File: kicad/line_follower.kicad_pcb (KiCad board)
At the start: 2 copper layers, 80 x 100 mm, 39 parts, among them J1 XT30PW-M, M1 MOTOR_ENC, M2 MOTOR_ENC, Q1 ALS-PT19-315C_L177_TR8, Q2 ALS-PT19-315C_L177_TR8, Q3 ALS-PT19-315C_L177_TR8, Q4 ALS-PT19-315C_L177_TR8, Q5 ALS-PT19-315C_L177_TR8, SW1 SW_Push, U1 A4950E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

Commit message: Getting there with the PCB design.
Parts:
- added HS1: Heatsink_Pad, cube-library:3x3_thermal_vias, F.Cu at (22.9, 1.27)
- added HS2: Heatsink_Pad, cube-library:3x3_thermal_vias, F.Cu at (-12.7, 1.27)
- added HS3: Heatsink_Pad, cube-library:3x3_thermal_vias, F.Cu at (-22.9, 1.27)
- added HS4: Heatsink_Pad, cube-library:3x3_thermal_vias, F.Cu at (12.7, 1.27)
- moved R7 43.2 mm to (21.6, 41.9), turned to 0 degrees
- moved C10 39.2 mm to (-31.8, 38.1)
- moved R6 38.3 mm to (16.5, 41.9)
- moved C11 30.3 mm to (-31.8, 27.9)
- moved U3 29.8 mm to (-31.8, 33.0), turned to 0 degrees
- moved X3 26.9 mm to (29.2, 58.4), turned to 90 degrees
- moved M2 22.2 mm to (-14.0, -8.26)
- moved M1 21.9 mm to (14.0, -8.26)
- moved C6 20.1 mm to (12.7, -2.54), turned to 270 degrees
- moved C9 12.8 mm to (-5.71, -1.27), turned to 180 degrees
- moved U2 10.8 mm to (-17.8, 0.00), turned to 90 degrees
- moved D1 10.8 mm to (24.7, 78.2)
- moved R1 10.2 mm to (21.6, 58.4)
- moved R2 10.2 mm to (16.5, 58.4)
- moved R3 10.2 mm to (11.4, 58.4)
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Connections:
- net /LINE_SENSOR1 renamed LINE_SENSOR1
- net /LINE_SENSOR2 renamed LINE_SENSOR2
- C1 pad 2: /LINE_SENSOR0 -> LINE_SENSOR0
- C4 pad 2: /LINE_SENSOR3 -> LINE_SENSOR3
- C5 pad 2: /LINE_SENSOR4 -> LINE_SENSOR4
- D1 pad 1: /LINE_LED1 -> LINE_LED1
- D1 pad 2: /LINE_LED0 -> LINE_LED0
- D2 pad 1: /LINE_LED0 -> LINE_LED0
- D2 pad 2: /LINE_LED1 -> LINE_LED1
- D3 pad 1: /LINE_LED2 -> LINE_LED2
- D3 pad 2: /LINE_LED0 -> LINE_LED0
- D4 pad 1: /LINE_LED0 -> LINE_LED0
- D4 pad 2: /LINE_LED2 -> LINE_LED2
- D5 pad 1: /LINE_LED1 -> LINE_LED1
- D5 pad 2: /LINE_LED2 -> LINE_LED2
- D6 pad 1: /LINE_LED2 -> LINE_LED2
- D6 pad 2: /LINE_LED1 -> LINE_LED1
- Q1 pad 2: /LINE_SENSOR0 -> LINE_SENSOR0
- Q4 pad 2: /LINE_SENSOR3 -> LINE_SENSOR3
- Q5 pad 2: /LINE_SENSOR4 -> LINE_SENSOR4
- R1 pad 2: /LINE_SENSOR0 -> LINE_SENSOR0
- R4 pad 2: /LINE_SENSOR3 -> LINE_SENSOR3
- R5 pad 2: /LINE_SENSOR4 -> LINE_SENSOR4
- U1 pad 4: +5V -> +3V3
- U2 pad 4: +5V -> +3V3
- X1 pad 10: /LINE_LED2 -> LINE_LED0
- X1 pad 11: /LINE_SENSOR3 -> /RANGE
- X1 pad 12: /MOTOR2A -> /MOTOR1B
- X1 pad 13: /MOTOR2B -> /MOTOR1A
- X1 pad 2: /ENCODER1B -> /ENCODER2A
- X1 pad 21: /ENCODER2B -> /ENCODER1A
- X1 pad 22: /ENCODER2A -> /ENCODER1B
- X1 pad 25: /MOTOR1A -> /MOTOR2B
- X1 pad 3: /ENCODER1A -> /ENCODER2B
- X1 pad 30: /MOTOR1B -> /MOTOR2A
- X1 pad 4: /LINE_SENSOR0 -> LINE_SENSOR4
- X1 pad 5: /RANGE -> LINE_SENSOR3
- X1 pad 7: /LINE_SENSOR4 -> LINE_SENSOR0
- X1 pad 8: /LINE_LED0 -> LINE_LED1
- X1 pad 9: /LINE_LED1 -> LINE_LED2
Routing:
- net GND: track 0.00 -> 415.5 mm, vias 0 -> 3
- net +3V3: track 0.00 -> 228.1 mm, vias 0 -> 7
- net +BATT: track 0.00 -> 187.5 mm, vias 0 -> 4
- net +5V: track 0.00 -> 142.3 mm
- net /ENCODER2A: track 0.00 -> 102.5 mm
- net /ENCODER2B: track 0.00 -> 101.1 mm
- net /MOTOR1A: track 0.00 -> 69.6 mm, vias 0 -> 1
- net /MOTOR1B: track 0.00 -> 69.1 mm, vias 0 -> 1
- net LINE_LED1: track 0.00 -> 68.2 mm, vias 0 -> 4
- net LINE_LED2: track 0.00 -> 62.7 mm, vias 0 -> 4
- net LINE_LED0: track 0.00 -> 61.7 mm, vias 0 -> 4
- net /ENCODER1A: track 0.00 -> 57.7 mm
- net /ENCODER1B: track 0.00 -> 56.6 mm
- net /MOTOR2B: track 0.00 -> 56.5 mm
- net /MOTOR2A: track 0.00 -> 45.8 mm
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- added copper zone on B.Cu, net GND
- added copper zone on F.Cu, net GND
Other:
- outline, holes or cut-outs redrawn

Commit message: Board done except for the motor mounts
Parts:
- added H1: MountingHole, MountingHole:MountingHole_3.2mm_M3, F.Cu at (0.00, -8.26)
- added H2: MountingHole, MountingHole:MountingHole_3.2mm_M3, F.Cu at (-29.8, -6.35)
- added H3: MountingHole, MountingHole:MountingHole_3.2mm_M3, F.Cu at (-29.2, 11.4)
- added H4: MountingHole, MountingHole:MountingHole_3.2mm_M3, F.Cu at (29.2, -6.35)
- added H5: MountingHole, MountingHole:MountingHole_3.2mm_M3, F.Cu at (29.2, 10.8)
- M1, M2: footprint cube-library:SolderWirePad1x6_p2.54 -> cube-library:SolderWirePad2x3_p2.54_staggered
- moved R6 8.89 mm to (16.5, 50.8)
- moved R7 8.89 mm to (21.6, 50.8)
- moved C8 5.08 mm to (5.71, 3.81), turned to 270 degrees
- moved C9 5.08 mm to (-5.71, 3.81), turned to 270 degrees
- moved M2 3.86 mm to (-17.8, -8.89)
- moved M1 2.62 mm to (16.5, -8.89)
- moved SW1 1.27 mm to (0.00, 7.62), turned to 270 degrees
- moved C10 0.63 mm to (-32.4, 38.1)
- moved C11 0.63 mm to (-32.4, 27.9)
- renumbered HS4 to HS2, HS2 to HS4
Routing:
- net GND: track 415.5 -> 381.6 mm, vias 3 -> 5
- net +3V3: track 228.1 -> 213.4 mm, vias 7 -> 5
- net +BATT: track 187.5 -> 178.9 mm
- net /ENCODER1B: track 56.6 -> 64.3 mm
- net Net-(M2-Pad6): track 12.0 -> 5.61 mm
- net /ENCODER1A: track 57.7 -> 63.2 mm
- net Net-(M1-Pad1): track 13.9 -> 8.76 mm
- net /BUTTON: track 42.1 -> 44.1 mm
- net Net-(M2-Pad1): track 5.61 -> 7.41 mm
- net LINE_LED0: track 61.7 -> 59.9 mm
- net LINE_LED2: track 62.7 -> 61.2 mm
- net /ACCEL_INT: track 28.0 -> 29.5 mm
- net +5V: track 142.3 -> 140.9 mm
- net /MOTOR1B: track 69.1 -> 70.4 mm
- net /BAT_SENSE: track 6.84 -> 8.11 mm
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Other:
- board text added: "6V-17V (2S-4S LiPo)"
- board text added: "JLCJLCJLCJLC"
- board text added: "Line Follower v2 https://github.com/bluecube August 2020"

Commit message: Small PCB tweaks
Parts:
- moved C6 1.27 mm to (14.0, -2.54)
- moved HS4 1.27 mm to (-14.0, 1.27)
- moved C7 1.27 mm to (-24.1, -2.54)
- moved HS1 1.27 mm to (24.1, 1.27)
- moved HS3 1.27 mm to (-24.1, 1.27)
- moved M1 1.27 mm to (17.8, -8.89)
- moved M2 1.27 mm to (-19.1, -8.89)
- moved U1 1.27 mm to (19.1, 0.00)
- moved U2 1.27 mm to (-19.1, 0.00)
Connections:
- J1 pad 3: Net-(J1-Pad3) -> GND
- J1 pad 4: Net-(J1-Pad4) -> GND
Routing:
- net GND: track 381.6 -> 418.2 mm, vias 5 -> 4
- net +BATT: track 178.9 -> 181.4 mm
- net /ENCODER2A: track 103.1 -> 104.4 mm
- net /ENCODER1B: track 64.3 -> 65.6 mm
- net /ENCODER1A: track 63.2 -> 64.5 mm
- net /ENCODER2B: track 101.7 -> 103.0 mm
- net +3V3: track 213.4 -> 214.2 mm
- net /ACCEL_INT: track 29.5 -> 28.8 mm
- net /MOTOR1A: track 69.6 -> 69.1 mm
- net /MOTOR2A: track 45.8 -> 46.3 mm
- net /MOTOR2B: track 55.8 -> 56.3 mm

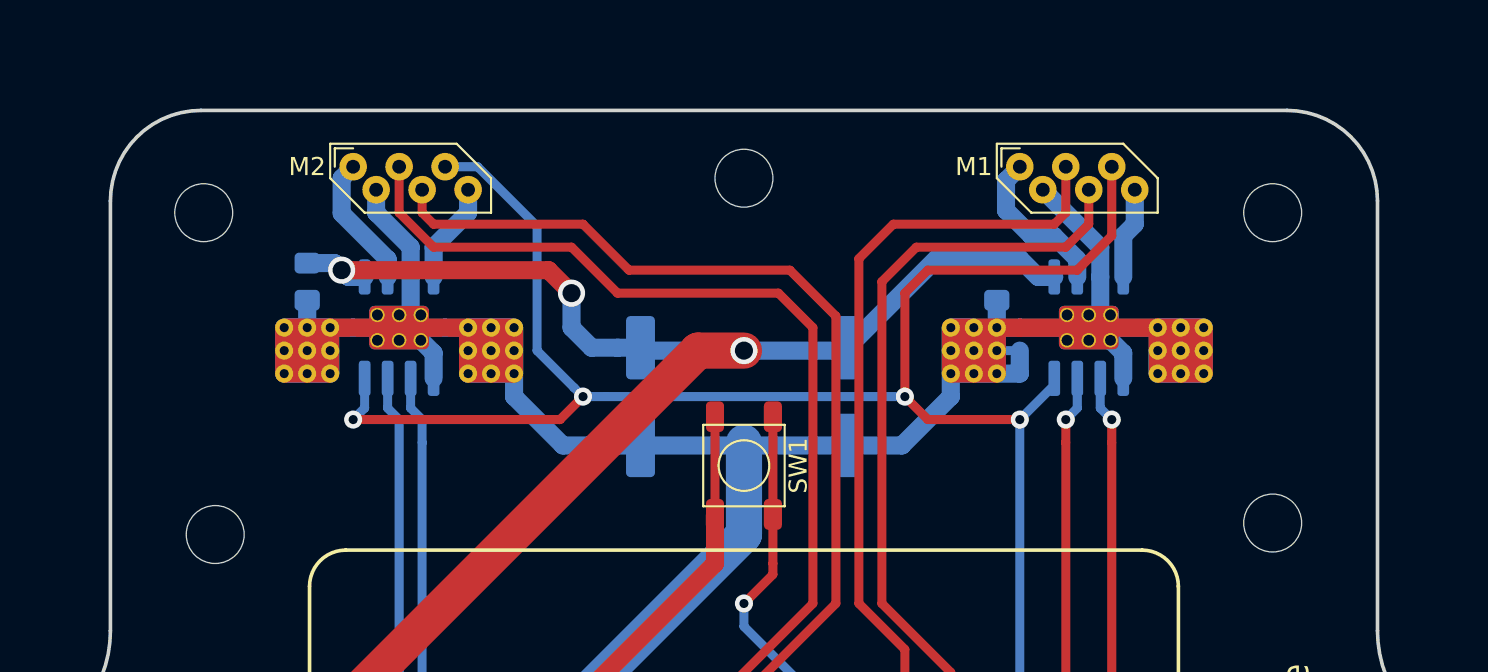
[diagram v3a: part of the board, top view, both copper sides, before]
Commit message: Placed motor mounting holes and silkscreen outlines.
Board done for now.
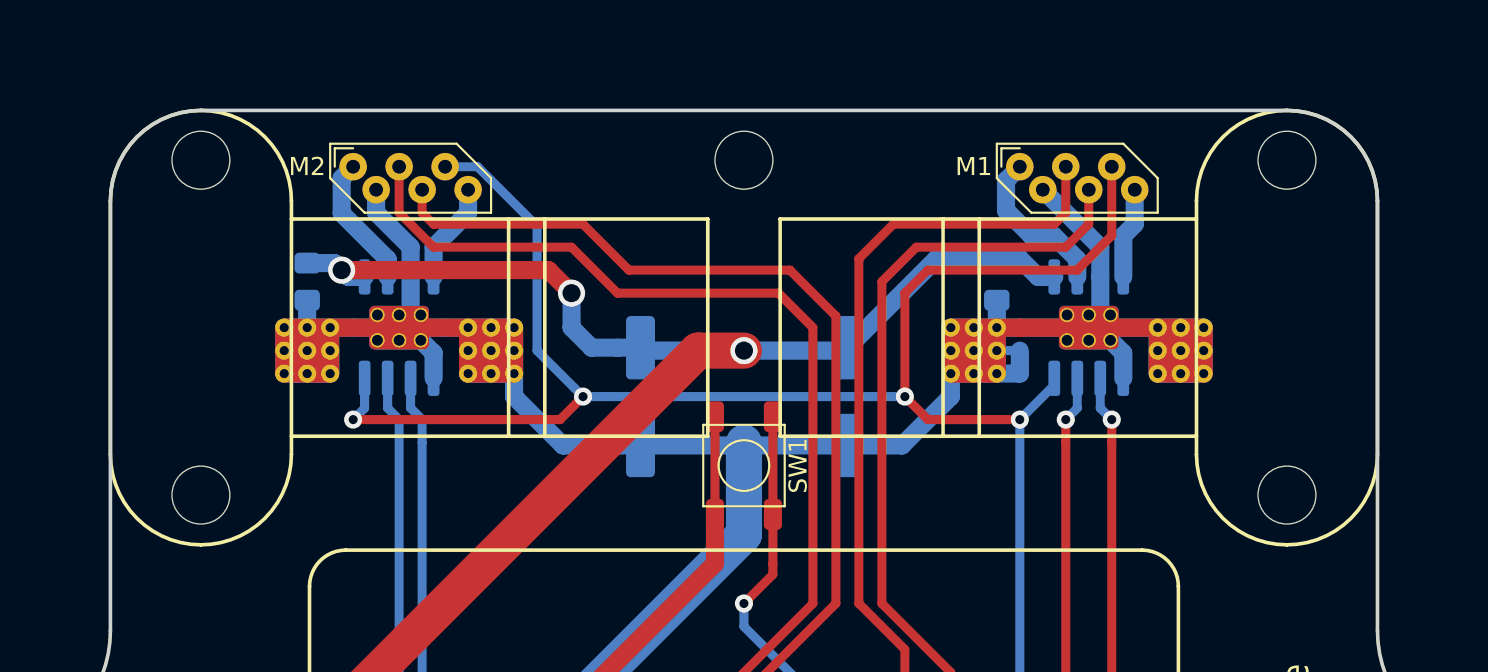
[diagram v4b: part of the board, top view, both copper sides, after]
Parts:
- moved H4 3.01 mm to (30.0, -9.25)
- moved H2 2.90 mm to (-30.0, -9.25)
- moved H3 2.32 mm to (-30.0, 9.25)
- moved H5 1.74 mm to (30.0, 9.25)
- moved H1 0.99 mm to (0.00, -9.25)
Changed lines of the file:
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@@
   (general
     (thickness 1.6)
-    (drawings 33)
+    (drawings 59)
     (tracks 499)
     (zones 0)
@@
   )
   (module MountingHole:MountingHole_3.2mm_M3 (layer F.Cu)
-    (at -29.845 -6.35)
+    (at -30 -9.25)
     (descr "Mounting Hole 3.2mm, no annular, M3")
     (tags "mounting hole 3.2mm no annular m3")
@@
   )
   (module MountingHole:MountingHole_3.2mm_M3 (layer F.Cu)
-    (at -29.21 11.43)
+    (at -30 9.25)
     (descr "Mounting Hole 3.2mm, no annular, M3")
     (tags "mounting hole 3.2mm no annular m3")
@@
   )
   (module MountingHole:MountingHole_3.2mm_M3 (layer F.Cu)
-    (at 29.21 -6.35)
+    (at 30 -9.25)
     (descr "Mounting Hole 3.2mm, no annular, M3")
     (tags "mounting hole 3.2mm no annular m3")
@@
   )
   (module MountingHole:MountingHole_3.2mm_M3 (layer F.Cu)
-    (at 29.21 10.795)
+    (at 30 9.25)
     (descr "Mounting Hole 3.2mm, no annular, M3")
     (tags "mounting hole 3.2mm no annular m3")
@@
   )
   (module MountingHole:MountingHole_3.2mm_M3 (layer F.Cu)
-    (at 0 -8.255)
+    (at 0 -9.25)
     (descr "Mounting Hole 3.2mm, no annular, M3")
     (tags "mounting hole 3.2mm no annular m3")
@@
       (net 11 "Net-(M2-Pad1)"))
   )
+  (gr_arc (start 30 6.999999) (end 30 11.999999) (angle -90) (layer F.SilkS) (width 0.2))
+  (gr_line (start 35 6.999999) (end 35 -7) (layer F.SilkS) (width 0.2))
+  (gr_arc (start 30 -7) (end 35 -7) (angle -90) (layer F.SilkS) (width 0.2))
+  (gr_line (start 25 -7) (end 25 6.999999) (layer F.SilkS) (width 0.2))
+  (gr_arc (start 30 6.999999) (end 25 6.999999) (angle -90) (layer F.SilkS) (width 0.2))
+  (gr_arc (start 30 -7) (end 30 -12) (angle -90) (layer F.SilkS) (width 0.2))
+  (gr_line (start 25 -6) (end 12.999999 -6) (layer F.SilkS) (width 0.2))
+  (gr_line (start 12.999999 -6) (end 10.999999 -6) (layer F.SilkS) (width 0.2))
+  (gr_line (start 12.999999 6) (end 12.999999 -6) (layer F.SilkS) (width 0.2))
+  (gr_line (start 10.999999 -6) (end 10.999999 6) (layer F.SilkS) (width 0.2))
+  (gr_line (start 1.999999 6) (end 24.999999 6) (layer F.SilkS) (width 0.2))
+  (gr_line (start 1.999999 -6) (end 1.999999 6) (layer F.SilkS) (width 0.2))
+  (gr_line (start 10.999999 -6) (end 1.999999 -6) (layer F.SilkS) (width 0.2))
+  (gr_line (start -12.999999 -6) (end -10.999999 -6) (layer F.SilkS) (width 0.2))
+  (gr_line (start -25 -7) (end -25 6.999999) (layer F.SilkS) (width 0.2))
+  (gr_line (start -10.999999 -6) (end -1.999999 -6) (layer F.SilkS) (width 0.2))
+  (gr_line (start -25 -6) (end -12.999999 -6) (layer F.SilkS) (width 0.2))
+  (gr_line (start -12.999999 6) (end -12.999999 -6) (layer F.SilkS) (width 0.2))
+  (gr_line (start -10.999999 -6) (end -10.999999 6) (layer F.SilkS) (width 0.2))
+  (gr_line (start -35 6.999999) (end -35 -7) (layer F.SilkS) (width 0.2))
+  (gr_line (start -1.999999 6) (end -24.999999 6) (layer F.SilkS) (width 0.2))
+  (gr_line (start -1.999999 -6) (end -1.999999 6) (layer F.SilkS) (width 0.2))
+  (gr_arc (start -30 6.999999) (end -30 11.999999) (angle -90) (layer F.SilkS) (width 0.2))
+  (gr_arc (start -30 6.999999) (end -35 6.999999) (angle -90) (layer F.SilkS) (width 0.2))
+  (gr_arc (start -30 -7) (end -25 -7) (angle -90) (layer F.SilkS) (width 0.2))
+  (gr_arc (start -30 -7) (end -30 -12) (angle -90) (layer F.SilkS) (width 0.2))
   (gr_text "6V-17V\n(2S-4S LiPo)" (at -31.75 34.29 90) (layer F.SilkS)
     (effects (font (size 1.5 1.2) (thickness 0.25)) (justify left))

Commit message: Untangled routing at the front of the robot a bit, moved battery location
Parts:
- moved SW1 1.38 mm to (0.00, 9.00), turned to 180 degrees
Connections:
- X1 pad 11: /RANGE -> LINE_SENSOR1
- X1 pad 12: /MOTOR1B -> LINE_SENSOR3
- X1 pad 20: LINE_SENSOR1 -> /MOTOR1B
- X1 pad 5: LINE_SENSOR3 -> LINE_SENSOR2
- X1 pad 6: LINE_SENSOR2 -> LINE_LED1
- X1 pad 8: LINE_LED1 -> /RANGE
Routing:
- net /MOTOR1B: track 70.4 -> 44.8 mm
- net LINE_SENSOR1: track 42.2 -> 24.7 mm, vias 1 -> 0
- net LINE_SENSOR3: track 31.0 -> 48.0 mm, vias 0 -> 1
- net GND: track 418.2 -> 433.6 mm, vias 4 -> 8
- net /RANGE: track 27.5 -> 35.1 mm
- net LINE_SENSOR0: track 45.6 -> 40.5 mm
- net LINE_SENSOR2: track 30.3 -> 32.8 mm
- net /ENCODER1B: track 65.6 -> 63.4 mm
- net /BUTTON: track 44.1 -> 42.2 mm
- net /ENCODER1A: track 64.5 -> 62.9 mm
- net /ENCODER2B: track 103.0 -> 104.0 mm
- net /ENCODER2A: track 104.4 -> 105.5 mm

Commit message: board: A bit more tweaking
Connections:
- X1 pad 12: LINE_SENSOR3 -> /RANGE
- X1 pad 8: /RANGE -> LINE_SENSOR3
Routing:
- net LINE_SENSOR3: track 48.0 -> 37.9 mm
- net /RANGE: track 35.1 -> 25.0 mm
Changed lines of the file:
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@@
     (thickness 1.6)
     (drawings 59)
-    (tracks 503)
+    (tracks 500)
     (zones 0)
     (modules 48)
@@
       (net 14 /BUTTON))
     (pad 8 thru_hole oval (at 0 12.7) (size 1.2 2) (drill 0.9) (layers *.Cu *.Mask)
-      (net 24 /RANGE))
+      (net 33 LINE_SENSOR3))
     (pad 22 thru_hole oval (at 2.54 -12.7) (size 1.2 2) (drill 0.9) (layers *.Cu *.Mask)
       (net 8 /ENCODER1B))
@@
       (net 26 "Net-(X1-Pad19)"))
     (pad 12 thru_hole oval (at 10.16 12.7) (size 1.2 2) (drill 0.9) (layers *.Cu *.Mask)
-      (net 33 LINE_SENSOR3))
+      (net 24 /RANGE))
     (pad 18 thru_hole oval (at 12.7 -12.7) (size 1.2 2) (drill 0.9) (layers *.Cu *.Mask)
       (net 13 /BAT_SENSE))
@@
   (gr_arc (start -41.75 16.749999) (end -38.857142 22.848678) (angle -64.62306647) (layer Edge.Cuts) (width 0.2))
   (gr_line (start -35 -7) (end -35 16.749999) (layer Edge.Cuts) (width 0.2))
-  (via (at -2.54 77.47) (size 1) (drill 0.5) (layers F.Cu B.Cu) (net 1))
+  (via (at -2.54 76.835) (size 1) (drill 0.5) (layers F.Cu B.Cu) (net 1))
   (via (at -11.43 76.2) (size 1) (drill 0.5) (layers F.Cu B.Cu) (net 1))
   (segment (start -30.725 31.945) (end -29.65 33.02) (width 1) (layer B.Cu) (net 1))
@@
   (via (at -5.08 63.5) (size 1) (drill 0.5) (layers F.Cu B.Cu) (net 23))
   (segment (start 26.67 68.58) (end 26.67 72.39) (width 0.5) (layer F.Cu) (net 24))
-  (segment (start 25.4 73.66) (end 11.43 73.66) (width 0.5) (layer F.Cu) (net 24))
   (segment (start 26.67 72.39) (end 25.4 73.66) (width 0.5) (layer F.Cu) (net 24))
-  (segment (start 7.62 73.66) (end 11.43 73.66) (width 0.5) (layer F.Cu) (net 24))
   (segment (start 29.21 60.96) (end 29.21 66.04) (width 0.5) (layer F.Cu) (net 24))
   (segment (start 29.21 66.04) (end 26.67 68.58) (width 0.5) (layer F.Cu) (net 24))
-  (segment (start 6.35 72.39) (end 7.62 73.66) (width 0.5) (layer F.Cu) (net 24))
-  (segment (start 6.35 71.12) (end 6.35 72.39) (width 0.5) (layer F.Cu) (net 24))
+  (segment (start 25.4 73.66) (end 17.78 73.66) (width 0.5) (layer F.Cu) (net 24))
+  (segment (start 16.51 72.39) (end 16.51 71.12) (width 0.5) (layer F.Cu) (net 24))
+  (segment (start 17.78 73.66) (end 16.51 72.39) (width 0.5) (layer F.Cu) (net 24))
   (segment (start 3.81 46.99) (end 3.81 45.72) (width 0.5) (layer B.Cu) (net 25))
   (segment (start 2.54 48.26) (end 3.81 46.99) (width 0.5) (layer B.Cu) (net 25))
@@
   (segment (start 19.837595 78.714249) (end 19.837595 76.682405) (width 0.5) (layer B.Cu) (net 30))
   (via (at 20.32 76.2) (size 1) (drill 0.5) (layers F.Cu B.Cu) (net 30))
-  (segment (start 3.81 72.39) (end 3.81 71.12) (width 0.5) (layer F.Cu) (net 30))
-  (segment (start 5.08 73.66) (end 3.81 72.39) (width 0.5) (layer F.Cu) (net 30))
-  (segment (start 20.32 76.2) (end 8.89 76.2) (width 0.5) (layer F.Cu) (net 30))
-  (segment (start 8.89 76.2) (end 7.62 76.2) (width 0.5) (layer F.Cu) (net 30))
-  (segment (start 7.62 76.2) (end 5.08 73.66) (width 0.5) (layer F.Cu) (net 30))
+  (segment (start 8.89 76.2) (end 20.32 76.2) (width 0.5) (layer F.Cu) (net 30))
+  (segment (start 7.62 76.2) (end 8.89 76.2) (width 0.5) (layer F.Cu) (net 30))
+  (segment (start 3.81 72.39) (end 7.62 76.2) (width 0.5) (layer F.Cu) (net 30))
+  (segment (start 3.81 71.12) (end 3.81 72.39) (width 0.5) (layer F.Cu) (net 30))
   (segment (start 13.97 64.525) (end 15.485 64.525) (width 0.5) (layer B.Cu) (net 31))
   (segment (start 15.485 64.525) (end 16.51 63.5) (width 0.5) (layer B.Cu) (net 31))
@@
   (segment (start 1.27 66.04) (end 3.81 66.04) (width 0.5) (layer B.Cu) (net 33))
   (segment (start -2.54 69.85) (end 1.27 66.04) (width 0.5) (layer B.Cu) (net 33))
-  (segment (start 16.51 68.58) (end 16.51 71.12) (width 0.5) (layer F.Cu) (net 33))
-  (segment (start 13.97 66.04) (end 16.51 68.58) (width 0.5) (layer F.Cu) (net 33))
-  (segment (start 3.81 66.04) (end 13.97 66.04) (width 0.5) (layer F.Cu) (net 33))
+  (segment (start 6.35 68.58) (end 3.81 66.04) (width 0.5) (layer F.Cu) (net 33))
+  (segment (start 6.35 71.12) (end 6.35 68.58) (width 0.5) (layer F.Cu) (net 33))
   (segment (start -1.27 64.525) (end 0.245 64.525) (width 0.5) (layer B.Cu) (net 34))
   (segment (start 1.27 63.5) (end 1.27 59.445) (width 0.5) (layer B.Cu) (net 34))
@@
   (segment (start 23.349789 79.229789) (end 22.86 78.74) (width 0.5) (layer B.Cu) (net 36))
   (via (at 22.86 78.74) (size 1) (drill 0.5) (layers F.Cu B.Cu) (net 36))
-  (segment (start 1.27 71.12) (end 1.27 74.93) (width 0.5) (layer F.Cu) (net 36))
   (segment (start -24.13 74.93) (end 1.27 74.93) (width 0.5) (layer F.Cu) (net 36))
   (segment (start 3.81 74.93) (end 1.27 74.93) (width 0.5) (layer F.Cu) (net 36))
@@
   (segment (start 6.35 77.47) (end 3.81 74.93) (width 0.5) (layer F.Cu) (net 36))
   (segment (start 22.86 78.74) (end 21.59 77.47) (width 0.5) (layer F.Cu) (net 36))
+  (segment (start 1.27 71.12) (end 1.27 74.93) (width 0.5) (layer F.Cu) (net 36))
   (segment (start -24.657875 79.229789) (end -23.640211 79.229789) (width 0.5) (layer B.Cu) (net 37))
   (segment (start -23.640211 79.229789) (end -22.86 80.01) (width 0.5) (layer B.Cu) (net 37))
